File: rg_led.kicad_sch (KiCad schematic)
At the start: 7 parts, among them Q200 PJE138K, Q201 PJE138K

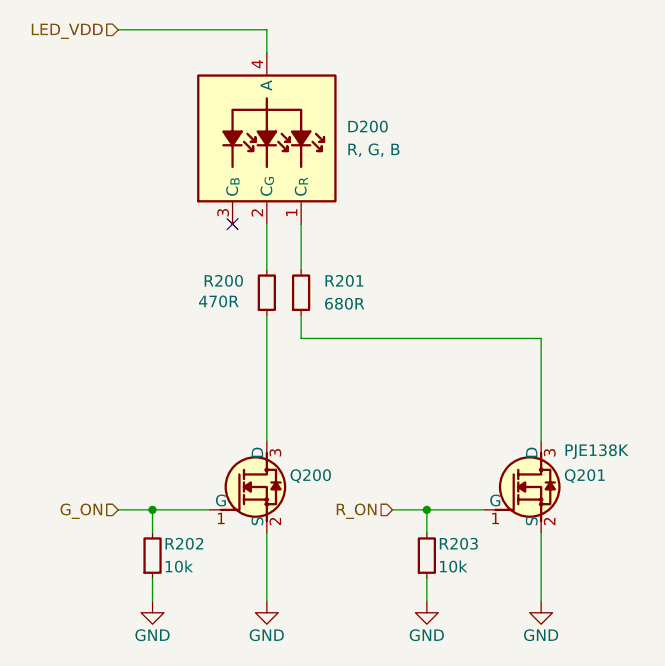
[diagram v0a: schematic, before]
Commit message: [#77400] Add grounded mounting pad
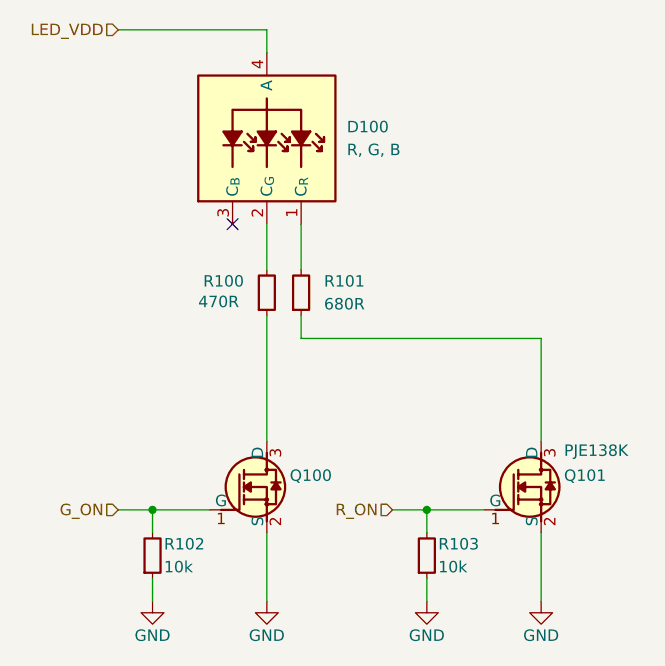
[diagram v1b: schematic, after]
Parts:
- renumbered D200 to D100, Q200 to Q100, Q201 to Q101, R200 to R100, R201 to R101, R202 to R102, R203 to R103
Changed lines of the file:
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@@
 	(title_block
 		(title "Jetson Orin Baseboard Test Rig")
-		(date "2025-05-16")
+		(date "2025-05-26")
 		(rev "1.0.0")
 		(company "Antmicro Ltd")
@@
 		(on_board yes)
 		(dnp no)
-		(property "Reference" "#PWR056"
+		(property "Reference" "#PWR070"
 			(at 193.04 177.8 0)
 			(effects
@@
 		(on_board yes)
 		(dnp no)
-		(property "Reference" "Q201"
+		(property "Reference" "Q101"
 			(at 234.95 161.29 0)
 			(effects
@@
 		(on_board yes)
 		(dnp no)
-		(property "Reference" "R203"
+		(property "Reference" "R103"
 			(at 220.98 168.91 90)
 			(effects
@@
 		(dnp no)
 		(fields_autoplaced yes)
-		(property "Reference" "D200"
+		(property "Reference" "D100"
 			(at 210.82 122.5549 90)
 			(effects
@@
 		(on_board yes)
 		(dnp no)
-		(property "Reference" "R200"
+		(property "Reference" "R100"
 			(at 199.39 139.7 90)
 			(do_not_autoplace yes)
@@
 		(on_board yes)
 		(dnp no)
-		(property "Reference" "#PWR061"
+		(property "Reference" "#PWR071"
 			(at 210.82 177.8 0)
 			(effects
@@
 		(on_board yes)
 		(dnp no)
-		(property "Reference" "Q200"
+		(property "Reference" "Q100"
 			(at 204.47 161.29 0)
 			(effects
@@
 		(on_board yes)
 		(dnp no)
-		(property "Reference" "#PWR055"
+		(property "Reference" "#PWR069"
 			(at 180.34 177.8 0)
 			(effects
@@
 		(on_board yes)
 		(dnp no)
-		(property "Reference" "#PWR062"
+		(property "Reference" "#PWR072"
 			(at 223.52 177.8 0)
 			(effects
@@
 		(dnp no)
 		(fields_autoplaced yes)
-		(property "Reference" "R201"
+		(property "Reference" "R101"
 			(at 208.28 139.7 90)
 			(effects
@@
 		(on_board yes)
 		(dnp no)
-		(property "Reference" "R202"
+		(property "Reference" "R102"
 			(at 190.5 168.91 90)
 			(effects
